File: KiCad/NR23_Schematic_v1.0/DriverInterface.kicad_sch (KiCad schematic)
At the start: 1 part

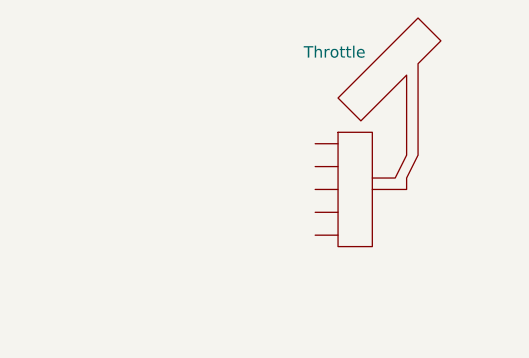
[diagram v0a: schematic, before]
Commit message: icc - throttle update
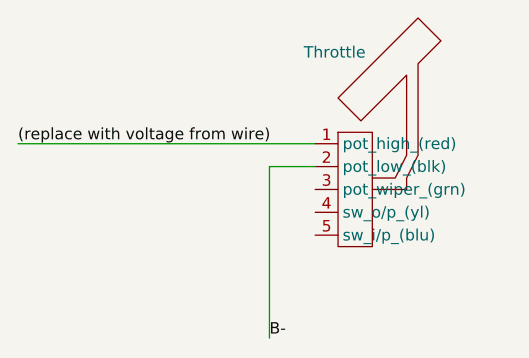
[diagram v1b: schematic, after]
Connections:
- new net (replace with voltage from wire): U?.1 (pot_high_(red))
- new net B-: U?.2 (pot_low_(blk))
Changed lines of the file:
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@@
 (kicad_sch (version 20211123) (generator eeschema)
   (paper "A4")
+  (wire (pts (xy 91.44 88.9) (xy 124.46 88.9))
+    (stroke (width 0) (type default) (color 0 0 0 0))
+  )
+  (wire (pts (xy 119.38 91.44) (xy 119.38 110.49))
+    (stroke (width 0) (type default) (color 0 0 0 0))
+  )
+  (wire (pts (xy 124.46 91.44) (xy 119.38 91.44))
+    (stroke (width 0) (type default) (color 0 0 0 0))
+  )
+  (label "B-" (at 119.38 110.49 0)
+    (effects (font (size 1.27 1.27)) (justify left bottom))
+  )
+  (label "(replace with voltage from wire)" (at 91.44 88.9 0)
+    (effects (font (size 1.27 1.27)) (justify left bottom))
+  )
   (symbol (lib_id "CamachosSymbols:Throttle") (at 134.62 90.17 0) (unit 1)
     (in_bom yes) (on_board yes)
@@
       (effects (font (size 1.27 1.27)) hide)
     )
-    (pin "")
-    (pin "")
-    (pin "")
-    (pin "")
-    (pin "")
+    (pin "5")
+    (pin "4")
+    (pin "3")
+    (pin "2")
+    (pin "1")
   )
 )

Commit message: fixed throttle
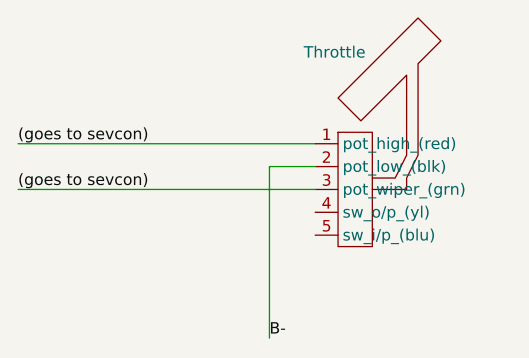
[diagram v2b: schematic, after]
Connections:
- net (replace with voltage from wire) is gone; now on net (goes to sevcon): U?.1 (pot_high_(red))
- net (goes to sevcon): now reaches U?.3 (pot_wiper_(grn))
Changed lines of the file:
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@@
+    (stroke (width 0) (type default) (color 0 0 0 0))
+  )
+  (wire (pts (xy 91.44 93.98) (xy 124.46 93.98))
     (stroke (width 0) (type default) (color 0 0 0 0))
   )
@@
     (effects (font (size 1.27 1.27)) (justify left bottom))
   )
-  (label "(replace with voltage from wire)" (at 91.44 88.9 0)
+  (label "(goes to sevcon)" (at 91.44 93.98 0)
     (effects (font (size 1.27 1.27)) (justify left bottom))
   )
+  (label "(goes to sevcon)" (at 91.44 88.9 0)
+    (effects (font (size 1.27 1.27)) (justify left bottom))
+  )

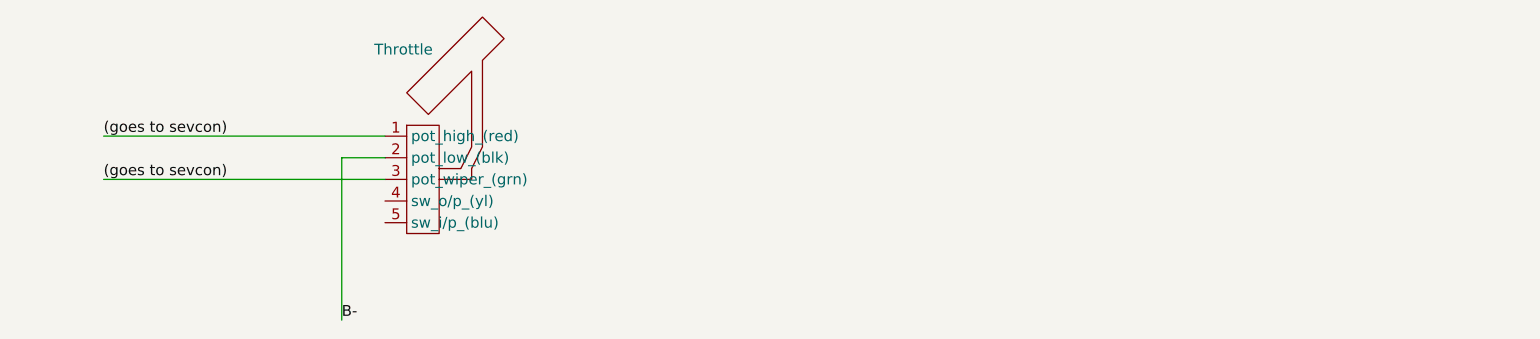
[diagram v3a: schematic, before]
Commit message: added fs1 to sevcon
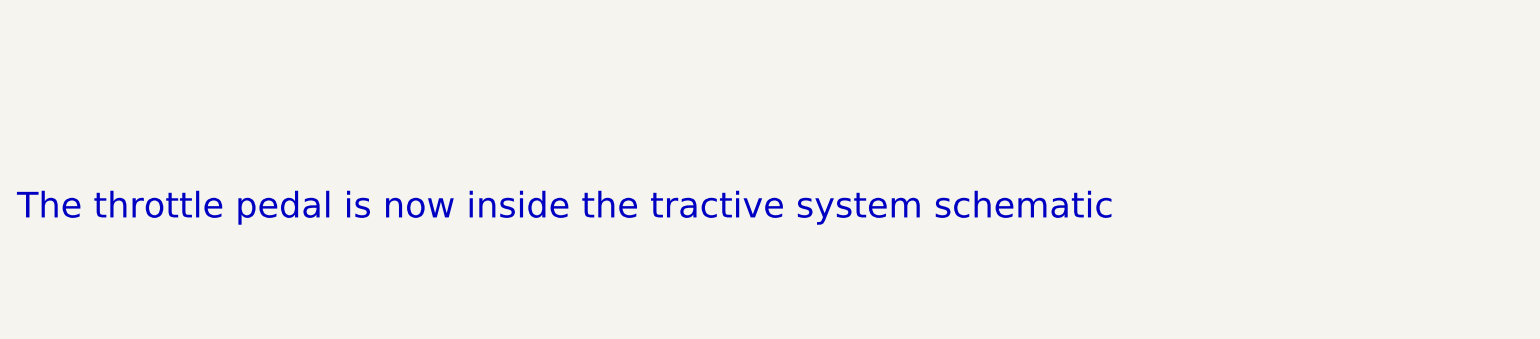
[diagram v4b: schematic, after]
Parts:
- removed U?: Throttle, symbol CamachosSymbols:Throttle
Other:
- note added: "The throttle pedal is now inside the tractive system schematic"
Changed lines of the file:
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@@
 (kicad_sch (version 20211123) (generator eeschema)
   (paper "A4")
-  (wire (pts (xy 91.44 88.9) (xy 124.46 88.9))
-    (stroke (width 0) (type default) (color 0 0 0 0))
-  )
-  (wire (pts (xy 91.44 93.98) (xy 124.46 93.98))
-    (stroke (width 0) (type default) (color 0 0 0 0))
-  )
-  (wire (pts (xy 119.38 91.44) (xy 119.38 110.49))
-    (stroke (width 0) (type default) (color 0 0 0 0))
-  )
-  (wire (pts (xy 124.46 91.44) (xy 119.38 91.44))
-    (stroke (width 0) (type default) (color 0 0 0 0))
-  )
-  (label "B-" (at 119.38 110.49 0)
-    (effects (font (size 1.27 1.27)) (justify left bottom))
-  )
-  (label "(goes to sevcon)" (at 91.44 93.98 0)
-    (effects (font (size 1.27 1.27)) (justify left bottom))
-  )
-  (label "(goes to sevcon)" (at 91.44 88.9 0)
-    (effects (font (size 1.27 1.27)) (justify left bottom))
-  )
-  (symbol (lib_id "CamachosSymbols:Throttle") (at 134.62 90.17 0) (unit 1)
-    (in_bom yes) (on_board yes)
-    (property "Reference" "U?" (id 0) (at 125.73 86.36 0)
-      (effects (font (size 1.27 1.27)) hide)
-    )
-    (property "Value" "Throttle" (id 1) (at 123.19 78.74 0)
-      (effects (font (size 1.27 1.27)) (justify left))
-    )
-    (property "Footprint" "" (id 2) (at 134.62 90.17 0)
-      (effects (font (size 1.27 1.27)) hide)
-    )
-    (property "Datasheet" "" (id 3) (at 134.62 90.17 0)
-      (effects (font (size 1.27 1.27)) hide)
-    )
-    (pin "1")
-    (pin "2")
-    (pin "3")
-    (pin "4")
-    (pin "5")
+  (text "The throttle pedal is now inside the tractive system schematic"
+    (at 81.28 99.06 0)
+    (effects (font (size 3 3)) (justify left bottom))
   )
 )
